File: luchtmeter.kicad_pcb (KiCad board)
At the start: 4 copper layers, 58 x 124 mm, 70 parts, among them J1 SCHERM, J2 USB-C, J3 I2C, J4 BATTERIJ, Q1 AO3401A, Q2 AO3401A, Q3 AO3400A, Q4 AO3400A, SW1 RESET, SW2 BOOT, SW3 WEKKEN, U1 ESP32-S3-WROOM-1-N16R8, U2 USBLC6-2SC6, U3 XC6220B331MR, U4 LTR-303ALS-01, U5 SCD41-D-R2, U6 SHT45, U7 BQ24075, U8 DW01A

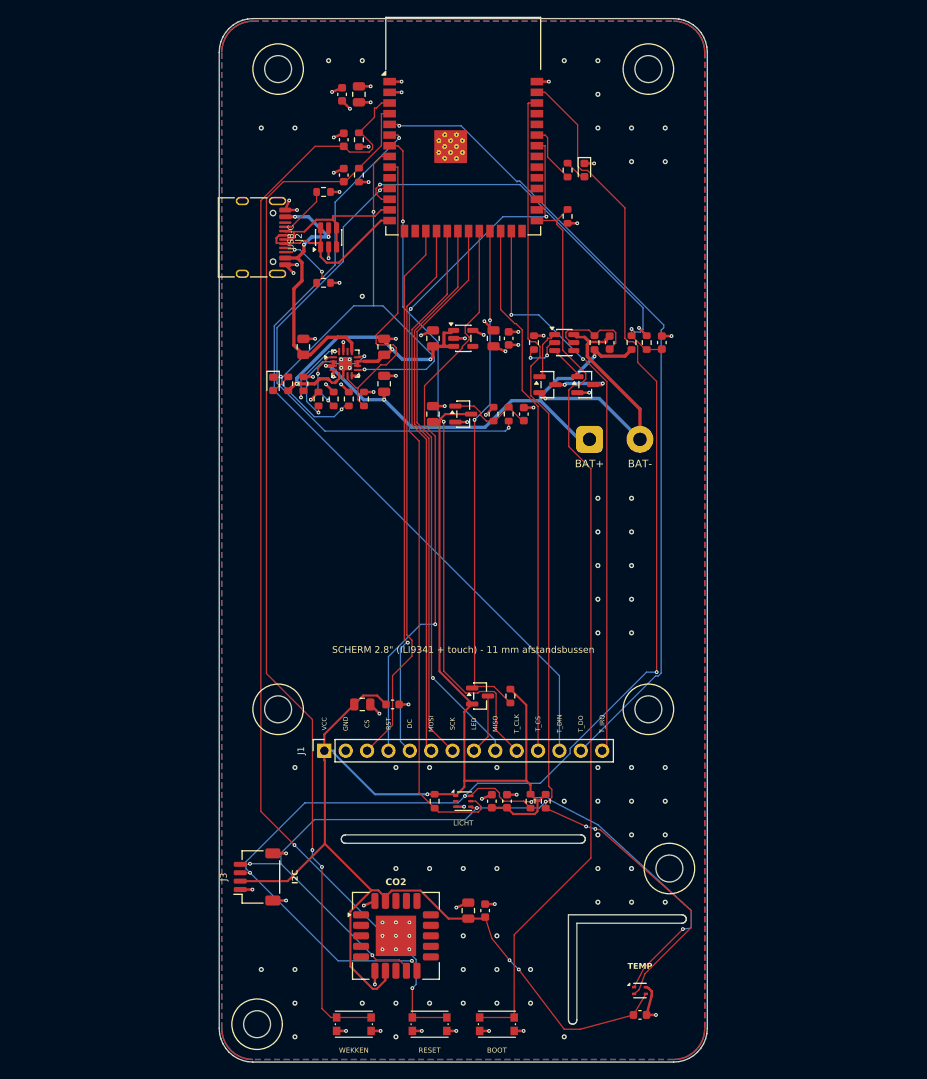
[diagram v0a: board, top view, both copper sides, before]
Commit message: Luchtmeter S3 v2: 4.3in Waveshare touchscreen (FFC), all parts on the back, NFC (ST25DV + PCB coil), WROOM-1U, TPS61023 screen boost, case + renders
Co-Authored-By: Claude Opus 5.5 <noreply@anthropic.com>
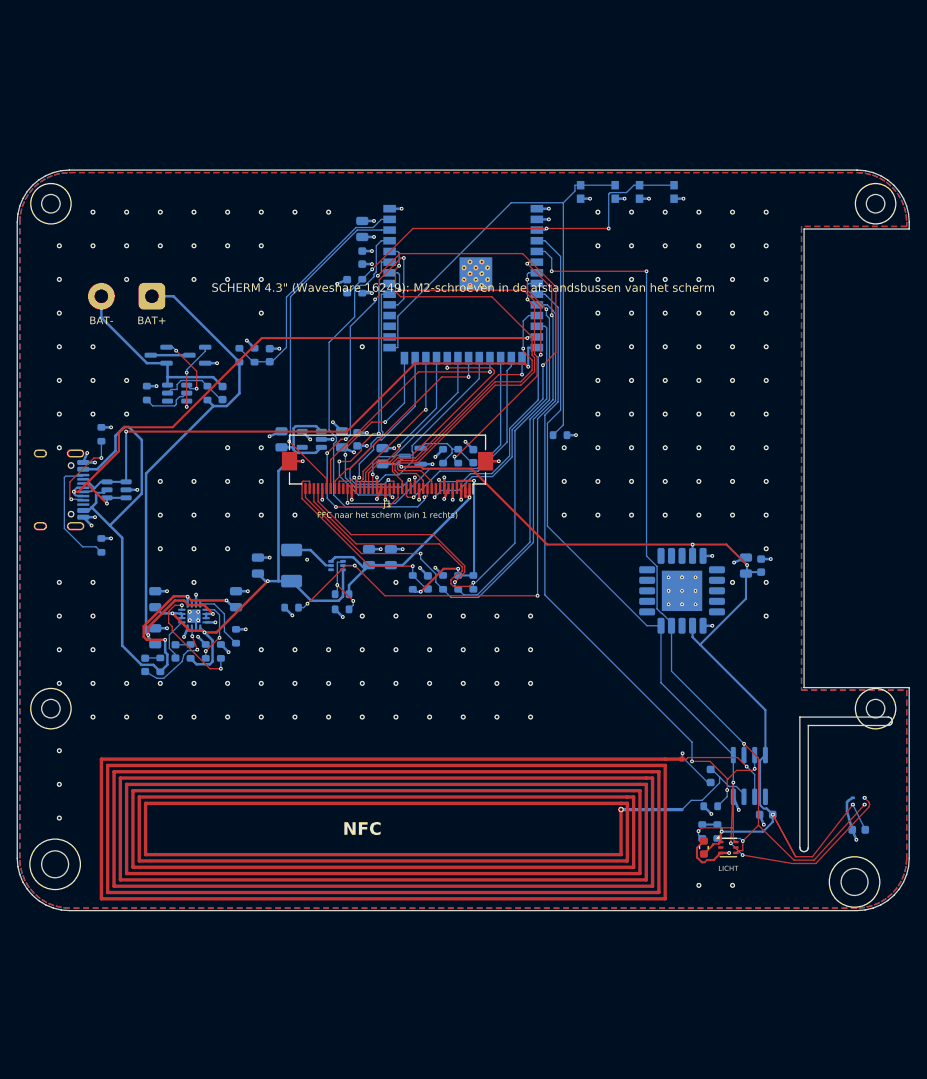
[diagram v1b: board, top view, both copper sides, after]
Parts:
- removed J3: I2C, lucht:JST_SH_SM04B-SRSS-TB_1x04-1MP_P1.00mm_Horizontal
- removed Q1: AO3401A, lucht:SOT-23
- removed SW3: WEKKEN, lucht:SW_Push_1P1T_NO_CK_KMR2
- added ANT1: NFC antenne, lucht:NFC_Coil, F.Cu at (150.0, 100.0)
- added C22: 100n, lucht:C_0603_1608Metric, B.Cu at (186.0, 132.6)
- added C23: 10p, lucht:C_0603_1608Metric, B.Cu at (179.4, 128.0)
- added L1: 1uH, lucht:L_Sunlord_MWSA0402S, B.Cu at (129.6, 103.0)
- added R23: 4k7, lucht:R_0603_1608Metric, B.Cu at (178.4, 134.6)
- added R24: 4k7, lucht:R_0603_1608Metric, B.Cu at (180.2, 134.6)
- added R25: 100k, lucht:R_0603_1608Metric, B.Cu at (179.4, 131.6)
- added U10: ST25DV04K, lucht:SOIC-8_3.9x4.9mm_P1.27mm, B.Cu at (184.0, 128.0)
- added U9: TPS61023, lucht:SOT-563, B.Cu at (135.0, 103.0)
- C1, C2, C3, C8, J2, J4, Q2, Q3, Q4, R1, R14, R2, R4, R7, U2, U3, U5, U6, U7, U8: moved to B.Cu
- C10: value 1u -> 22u; footprint lucht:C_0603_1608Metric -> lucht:C_0805_2012Metric; moved to B.Cu
- C11, C21, C7: value 10u -> 100n; footprint lucht:C_0805_2012Metric -> lucht:C_0603_1608Metric; moved to B.Cu
- C12: value 100n -> 47n; moved to B.Cu
- C13, C14, C19, C9: value 100n -> 10u; footprint lucht:C_0603_1608Metric -> lucht:C_0805_2012Metric; moved to B.Cu
- C15: value 4u7 -> 22u; moved to B.Cu
- C16: value 10u -> 22u; moved to B.Cu
- C17: value 4u7 -> 1u; footprint lucht:C_0805_2012Metric -> lucht:C_0603_1608Metric; moved to B.Cu
- C20: value 47n -> 100n; moved to B.Cu
- C4: value 10u -> 4u7; moved to B.Cu
- C5: value 22u -> 10u; moved to B.Cu
- C6: value 100n -> 4u7; footprint lucht:C_0603_1608Metric -> lucht:C_0805_2012Metric; moved to B.Cu
- D1: value groen -> rood laden; moved to B.Cu
- D2: value rood laden -> groen USB; moved to B.Cu
- H1, H2, H3, H4: value M3 -> M2; footprint lucht:MountingHole_3.2mm_M3 -> lucht:MountingHole_2.2mm_M2
- J1: footprint lucht:PinSocket_1x14_P2.54mm_Vertical -> lucht:Hirose_FH12-40S-0.5SH_1x40-1MP_P0.50mm_Horizontal
- R10: value 100k -> 100; moved to B.Cu
- R11: value 3.6k -> 1k; moved to B.Cu
- R12: value 1.1k -> 1M; moved to B.Cu
- R13: value 10k -> 1M; moved to B.Cu
- R15: value 100k -> 10k; moved to B.Cu
- R16: value 1k -> 732k; moved to B.Cu
- R17: value 100 -> 100k; moved to B.Cu
- R18: value 1k -> 100k; moved to B.Cu
- R19, R20: value 1M -> 10k; moved to B.Cu
- R21: value 100k -> 4k7; moved to B.Cu
- R22: value 10k -> 4k7; moved to B.Cu
- R3: value 1k -> 5k1; moved to B.Cu
- R5: value 5k1 -> 3.6k; moved to B.Cu
- R6: value 10k -> 1.1k; moved to B.Cu
- R8, R9: value 4k7 -> 1k; moved to B.Cu
- SW1: value RESET -> WEKKEN; moved to B.Cu
- SW2: value BOOT -> RESET; moved to B.Cu
- U1: value ESP32-S3-WROOM-1-N16R8 -> ESP32-S3-WROOM-1U-N16R8; footprint lucht:ESP32-S3-WROOM-1 -> lucht:ESP32-S3-WROOM-1U; moved to B.Cu
- moved SW1 100.9 mm to (166.0, 58.6), turned to 180 degrees
- moved SW2 100.7 mm to (173.0, 58.6), turned to 180 degrees
- moved D1 75.1 mm to (115.8, 113.2), turned to 90 degrees
- moved C13 73.1 mm to (140.4, 90.0), turned to 90 degrees
- moved C21 70.7 mm to (197.0, 134.4), turned to 180 degrees
- moved R3 63.7 mm to (107.0, 87.4)
- moved C18 61.0 mm to (178.6, 136.5)
- moved C11 57.5 mm to (137.4, 88.0)
- moved C6 54.9 mm to (113.4, 111.4)
- moved J4 54.7 mm to (113.0, 71.0), turned to 180 degrees
- moved C12 54.0 mm to (151.2, 90.0)
- moved U5 53.3 mm to (176.0, 106.0), turned to 180 degrees
- moved C5 50.8 mm to (113.4, 107.0)
- moved C9 49.7 mm to (128.4, 88.0)
- moved R4 49.6 mm to (107.0, 100.6), turned to 90 degrees
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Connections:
- C10 pad 1: 3V3_SW -> 3V3
- C11 pad 1: 3V3_SW -> 3V3
- C12 pad 1: 3V3_SW -> PWR_G
- C12 pad 2: GND -> 3V3
- C14 pad 1: WAKE -> VSYS
- C15 pad 1: VBUS -> V5D
- C16 pad 1: VSYS -> V5D
- C17 pad 1: VBAT -> TP_RST
- C18 pad 1: DW_VCC -> 3V3_SW
- C18 pad 2: BATN -> GND
- C19 pad 1: VBAT_SENSE -> 3V3_SW
- C20 pad 1: PWR_G -> 3V3_SW
- C20 pad 2: 3V3 -> GND
- C4 pad 1: VSYS -> VBUS
- C5 pad 1: 3V3 -> VSYS
- C6 pad 1: 3V3 -> VBAT
- C7 pad 1: 3V3_SW -> DW_VCC
- C7 pad 2: GND -> BATN
- C8 pad 1: 3V3_SW -> VBAT_SENSE
- C9 pad 1: 3V3_SW -> VSYS
- D1 pad 1: GND -> CHG
- D1 pad 2: LED_ST_A -> LED_CHG_A
- D2 pad 1: CHG -> PGOOD
- D2 pad 2: LED_CHG_A -> LED_PG_A
- J1 pad 1: 3V3_SW -> V5D
- J1 pad 10: T_CLK -> LCD_R5
- J1 pad 11: T_CS -> LCD_R6
- J1 pad 12: T_DIN -> LCD_R7
- J1 pad 13: T_DO -> GND
- J1 pad 14: T_IRQ -> GND
- J1 pad 2: GND -> V5D
- J1 pad 3: LCD_CS -> GND
- J1 pad 4: LCD_RST -> TP_3V3
- J1 pad 5: LCD_DC -> GND
- J1 pad 6: LCD_MOSI -> GND
- J1 pad 7: LCD_SCK -> GND
- J1 pad 8: LCD_LED -> LCD_R3
- J1 pad 9: LCD_MISO -> LCD_R4
- R10 pad 1: 3V3 -> VBAT
- R10 pad 2: WAKE -> DW_VCC
- R11 pad 1: CH_ISET -> DW_CS
- R12 pad 1: CH_ILIM -> VBAT
- R12 pad 2: GND -> VBAT_SENSE
- R13 pad 1: CH_TS -> VBAT_SENSE
- R14 pad 1: CHG -> PWR_G
- R15 pad 1: PGOOD -> PWR_EN
- R15 pad 2: 3V3 -> PWR_G
- R16 pad 1: VSYS -> V5D
- R16 pad 2: LED_CHG_A -> BST_FB
- R17 pad 1: VBAT -> BST_FB
- R17 pad 2: DW_VCC -> GND
- R18 pad 1: DW_CS -> DISP_ON
- R19 pad 1: VBAT -> TP_3V3
- R19 pad 2: VBAT_SENSE -> TP_RST
- R20 pad 1: VBAT_SENSE -> TP_INT
- R21 pad 1: PWR_G -> SDA1
- R21 pad 2: 3V3 -> TP_3V3
- R22 pad 1: PWR_EN -> SCL1
- R22 pad 2: PWR_G -> TP_3V3
- R3 pad 1: LED_ST -> CC1
- R3 pad 2: LED_ST_A -> GND
- R4 pad 1: CC1 -> CC2
- R5 pad 1: CC2 -> CH_ISET
- R6 pad 1: LCD_BL -> CH_ILIM
- R6 pad 2: 3V3_SW -> GND
- R7 pad 1: ALS_INT -> CH_TS
- R7 pad 2: 3V3_SW -> GND
- R8 pad 1: SDA -> VSYS
- R8 pad 2: 3V3_SW -> LED_CHG_A
- R9 pad 1: SCL -> VBUS
- R9 pad 2: 3V3_SW -> LED_PG_A
- SW1 pad 1: ESP_EN -> ESP_IO0
- SW2 pad 1: ESP_IO0 -> ESP_EN
- U1 pad 10: unconnected-(U1-IO17-Pad10) -> DISP_ON
- U1 pad 11: PWR_EN -> LCD_R7
- U1 pad 12: VBAT_SENSE -> SCL1
- U1 pad 15: unconnected-(U1-IO3-Pad15) -> LCD_G4
- U1 pad 16: unconnected-(U1-IO46-Pad16) -> LCD_G3
- U1 pad 17: LCD_DC -> PCLK
- U1 pad 18: LCD_CS -> DE
- U1 pad 19: LCD_MOSI -> HSYNC
- U1 pad 20: LCD_SCK -> VSYNC
- U1 pad 21: LCD_MISO -> LCD_B3
- U1 pad 22: LCD_RST -> LCD_B4
- U1 pad 23: LCD_BL -> LCD_B5
- U1 pad 24: T_CS -> LCD_B6
- U1 pad 25: T_IRQ -> LCD_B7
- U1 pad 26: unconnected-(U1-IO45-Pad26) -> LCD_G2
- U1 pad 31: unconnected-(U1-IO38-Pad31) -> LCD_G5
- U1 pad 32: unconnected-(U1-IO39-Pad32) -> LCD_G6
- U1 pad 33: unconnected-(U1-IO40-Pad33) -> LCD_G7
- U1 pad 34: ALS_INT -> LCD_R3
- U1 pad 35: LED_ST -> LCD_R4
- U1 pad 36: unconnected-(U1-RXD0-Pad36) -> LCD_R5
- U1 pad 37: unconnected-(U1-TXD0-Pad37) -> LCD_R6
- U1 pad 38: SCL -> BL_PWM
- U1 pad 39: SDA -> VBAT_SENSE
- U1 pad 4: WAKE -> SDA0
- U1 pad 5: T_DO -> SCL0
- U1 pad 6: T_DIN -> TP_INT
- U1 pad 7: T_CLK -> SDA1
- U1 pad 8: CHG -> PWR_EN
- U1 pad 9: PGOOD -> NFC_GPO
- U4 pad 4: SCL -> SCL0
- U4 pad 5: ALS_INT -> unconnected-(U4-INT-Pad5)
- U4 pad 6: SDA -> SDA0
- U5 pad 10: SDA -> SDA0
- U5 pad 9: SCL -> SCL0
- U6 pad 1: SDA -> SDA0
- U6 pad 2: SCL -> SCL0
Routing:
- net SDA: track 208.8 -> 0.00 mm, vias 6 -> 0
- net SCL: track 183.1 -> 0.00 mm, vias 6 -> 0
- net WAKE: track 126.3 -> 0.00 mm, vias 2 -> 0
- net SDA0: track 0.00 -> 118.0 mm, vias 0 -> 5
- net SCL0: track 0.00 -> 112.7 mm, vias 0 -> 5
- net ALS_INT: track 98.4 -> 0.00 mm, vias 2 -> 0
- net T_DO: track 97.4 -> 0.00 mm, vias 1 -> 0
- net T_DIN: track 94.4 -> 0.00 mm, vias 1 -> 0
- net ESP_EN: track 134.3 -> 47.8 mm, vias 2 -> 3
- net T_CLK: track 80.9 -> 0.00 mm, vias 2 -> 0
- net NFC_GPO: track 0.00 -> 79.2 mm, vias 0 -> 3
- net TP_INT: track 0.00 -> 73.3 mm, vias 0 -> 3
- net 3V3_SW: track 203.7 -> 131.3 mm, vias 3 -> 6
- net SDA1: track 0.00 -> 72.1 mm, vias 0 -> 3
- net DISP_ON: track 0.00 -> 70.5 mm, vias 0 -> 3
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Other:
- board size 58 x 124 mm -> 106 x 88 mm
- board text added: "CO2 · temp · vocht · licht · NFC"
- board text added: "FFC naar het scherm (pin 1 rechts)"
- board text added: "Kobe Van Robaeys · 2026"
- board text added: "LUCHTMETER"
- board text added: "LiPo 300 mAh hier"
- board text added: "NFC"
- board text added: "SCHERM 4.3" (Waveshare 16249): M2-schroeven in de afstandsbussen van het scherm"
- board text added: "U.FL antenne"
- board text removed: "BOOT"
- board text removed: "CO2 · temperatuur · vocht · licht"
- board text removed: "CS"
- board text removed: "DC"
- board text removed: "ESP32-S3 + SCD41 + SHT45 + LTR-303 + 2.8" touch"
- board text removed: "GND"
- board text removed: "I2C"
- board text removed: "Kobe Van Robaeys · maakleerplek · 2026"
- board text removed: "LED"
- board text removed: "LUCHTMETER S3"
- board text removed: "MISO"
- board text removed: "MOSI"
- board text removed: "RST"
- board text removed: "SCHERM 2.8" (ILI9341 + touch) - 11 mm afstandsbussen"
- board text removed: "SCK"
- board text removed: "T_CLK"
- board text removed: "T_CS"
- board text removed: "T_DIN"
- board text removed: "T_DO"
- board text removed: "T_IRQ"
- board text removed: "VCC"

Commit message: Credit varol56 as co-inventor on silkscreen, schematic and firmware
Co-authored-by: varol56 <74546798+varol56@users.noreply.github.com>
Co-Authored-By: Claude Opus 5.5 <noreply@anthropic.com>
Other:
- board text added: "Kobe Van Robaeys & varol56 · 2026"
- board text removed: "Kobe Van Robaeys · 2026"
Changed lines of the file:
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@@
 		)
 	)
-	(gr_text "Kobe Van Robaeys · 2026"
+	(gr_text "Kobe Van Robaeys & varol56 · 2026"
 		(at 175.5 77 0)
 		(layer "B.SilkS")

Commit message: Name: Kobe Vanrobaeys (README, silkscreen, schematic, firmware, video)
Co-Authored-By: Claude Opus 5.5 <noreply@anthropic.com>
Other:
- board text added: "Kobe Vanrobaeys & varol56 · 2026"
- board text removed: "Kobe Van Robaeys & varol56 · 2026"
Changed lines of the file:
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@@
 		)
 	)
-	(gr_text "Kobe Van Robaeys & varol56 · 2026"
+	(gr_text "Kobe Vanrobaeys & varol56 · 2026"
 		(at 175.5 77 0)
 		(layer "B.SilkS")

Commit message: Rebuild board, schematic and fab outputs with test points (#1) and J3 (#2)
Regenerated from design.py with KiCad 10.0.7 (flatpak) on Linux:
libs.py, build_sch.py, build_pcb.py, route.sh (Freerouting 2.4.1), finisher,
parity.py fixnc, fab.py.

- TP1-TP13: 1.5 mm test pads in one row on the back, net names in silkscreen
- J3: 1x4 2.54 mm probe connector GND/TP_3V3/SDA1/SCL1 at the left edge next
  to the USB-C (DNP, not in BOM/CPL)

Checks: DRC 0 violations, 0 unconnected, 0 schematic parity issues;
ERC 0 errors 0 warnings; parity.py 314 pads, 0 mismatches. The SHT45 3V3_SW
link is now routed by the tools as well (no manual track).

Co-Authored-By: Claude <noreply@anthropic.com>
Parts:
- added J3: SONDE I2C1, lucht:PinHeader_1x04_P2.54mm_Vertical, B.Cu at (101.0, 103.2)
- added TP1: GND, lucht:TestPoint_Pad_D1.5mm, B.Cu at (151.0, 117.5)
- added TP10: SCL0, lucht:TestPoint_Pad_D1.5mm, B.Cu at (178.0, 117.5)
- added TP11: SDA1, lucht:TestPoint_Pad_D1.5mm, B.Cu at (181.0, 117.5)
- added TP12: SCL1, lucht:TestPoint_Pad_D1.5mm, B.Cu at (184.0, 117.5)
- added TP13: GND, lucht:TestPoint_Pad_D1.5mm, B.Cu at (187.0, 117.5)
- added TP2: VBUS, lucht:TestPoint_Pad_D1.5mm, B.Cu at (154.0, 117.5)
- added TP3: VBAT, lucht:TestPoint_Pad_D1.5mm, B.Cu at (157.0, 117.5)
- added TP4: VSYS, lucht:TestPoint_Pad_D1.5mm, B.Cu at (160.0, 117.5)
- added TP5: 3V3, lucht:TestPoint_Pad_D1.5mm, B.Cu at (163.0, 117.5)
- added TP6: 3V3_SW, lucht:TestPoint_Pad_D1.5mm, B.Cu at (166.0, 117.5)
- added TP7: V5D, lucht:TestPoint_Pad_D1.5mm, B.Cu at (169.0, 117.5)
- added TP8: TP_3V3, lucht:TestPoint_Pad_D1.5mm, B.Cu at (172.0, 117.5)
- added TP9: SDA0, lucht:TestPoint_Pad_D1.5mm, B.Cu at (175.0, 117.5)
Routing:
- net TP_3V3: track 23.5 -> 104.1 mm, vias 3 -> 6
- net SDA1: track 72.1 -> 150.1 mm, vias 3 -> 5
- net SCL1: track 64.2 -> 137.7 mm, vias 1 -> 3
- net V5D: track 27.1 -> 70.8 mm, vias 1 -> 2
- net VBAT: track 66.1 -> 108.0 mm, vias 2 -> 3
- net VSYS: track 68.7 -> 108.9 mm, vias 3 -> 5
- net VBUS: track 72.8 -> 98.5 mm, vias 3 -> 6
- net LCD_G5: track 50.1 -> 25.1 mm, vias 5 -> 1
- net 3V3_SW: track 131.3 -> 147.6 mm, vias 6 -> 5
- net LCD_R4: track 61.3 -> 47.4 mm, vias 3 -> 7
- net DISP_ON: track 70.5 -> 80.8 mm, vias 3 -> 2
- net LCD_B4: track 28.9 -> 20.2 mm
- net LCD_G7: track 35.7 -> 27.3 mm, vias 3 -> 1
- net DW_OD: track 8.20 -> 14.9 mm
- net SCL0: track 112.7 -> 119.1 mm
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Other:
- board text added: "3V3"
- board text added: "3V3_SW"
- board text added: "GND"
- board text added: "SCL0"
- board text added: "SCL1"
- board text added: "SDA0"
- board text added: "SDA1"
- board text added: "SONDE"
- board text added: "TESTPUNTEN"
- board text added: "TP_3V3"
- board text added: "V5D"
- board text added: "VBAT"
- board text added: "VBUS"
- board text added: "VSYS"
